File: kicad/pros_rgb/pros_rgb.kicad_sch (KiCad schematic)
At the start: 41 parts, among them Q73 N54D, U2 20RB, U3 HT32F1654, U5 GD25Q40CT, X1 8MHz

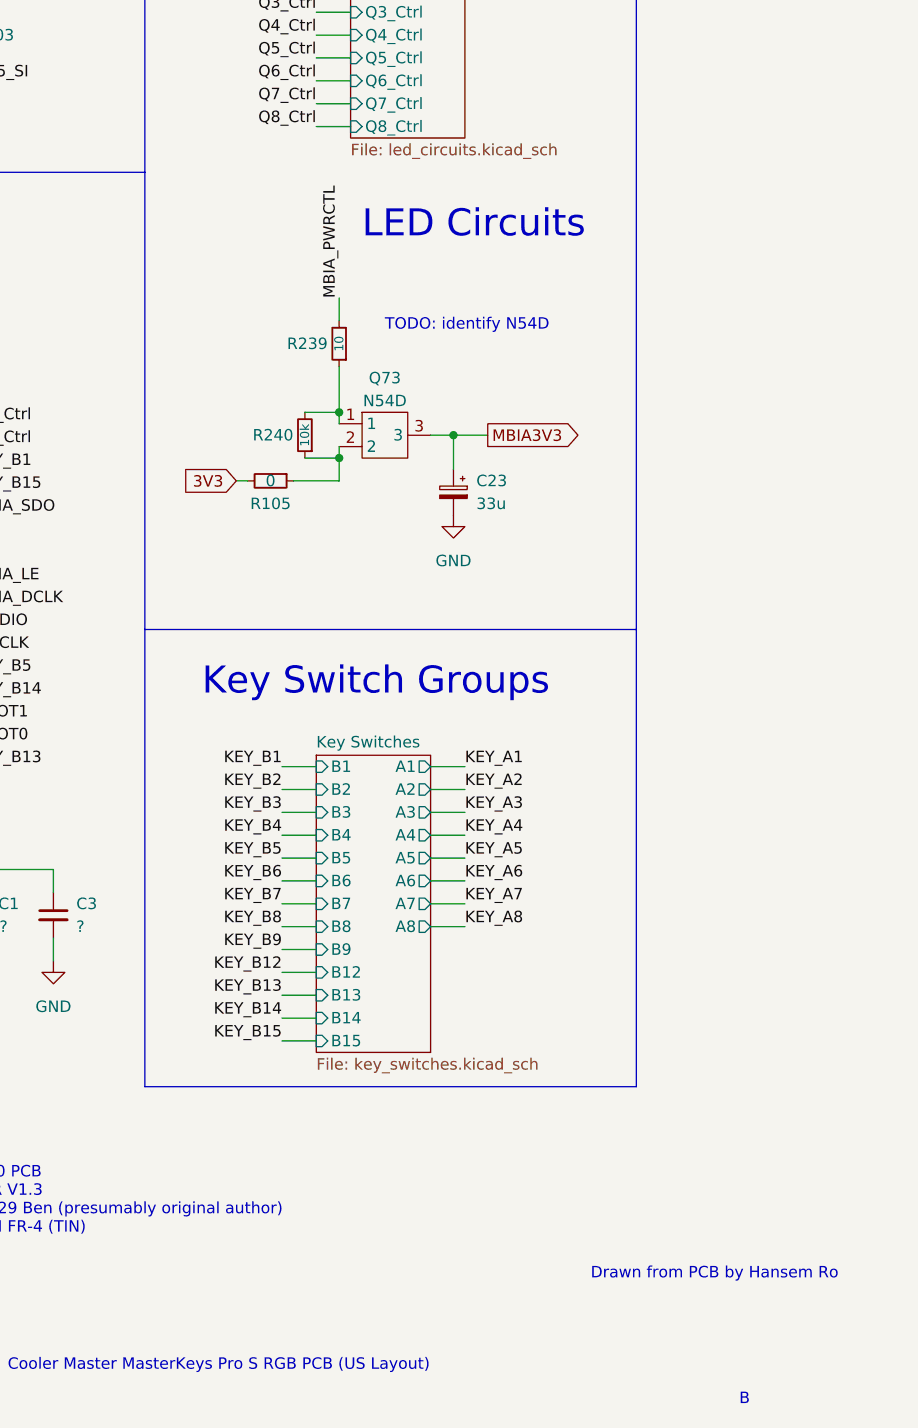
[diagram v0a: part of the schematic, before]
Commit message: kicad/pros_rgb: use pmos symbol for N54D
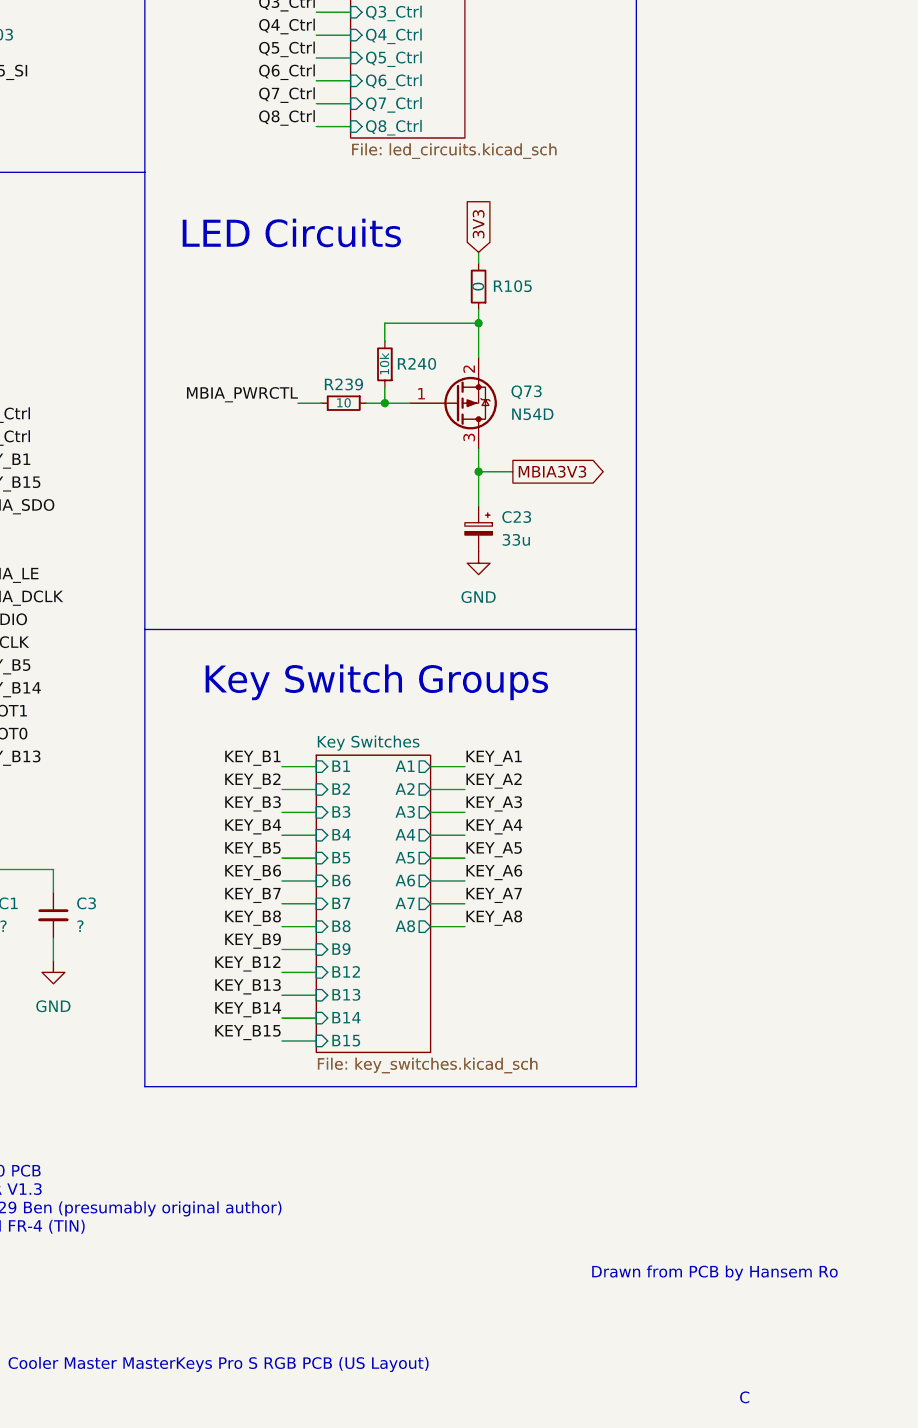
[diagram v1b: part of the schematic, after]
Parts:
- removed Q73: N54D, symbol SMD_components:N54D
- added Q73: N54D, symbol Device:Q_PMOS_GSD
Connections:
- net MBIA3V3: now also Q73.3 (D)
- net at R240.2: now also R105.1, Q73.2 (S); no longer R239.1
- net at R240.1: now also R239.1, Q73.1 (G); no longer R105.1
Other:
- note added: "C"
- note removed: "B"
- note removed: "TODO: identify N54D"
- moved on the sheet: C23, R105, R239, R240
